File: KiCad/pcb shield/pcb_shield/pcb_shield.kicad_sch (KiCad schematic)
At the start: 3 parts, among them J1 Raspberry Pi Zero, U1 BOB-09056

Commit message: add main parts
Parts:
- added A?: Motor Controller Left, Module:Pololu_Breakout-16_15.2x20.3mm, symbol Driver_Motor:Pololu_Breakout_A4988
- added A?: Motor Controller Right, Module:Pololu_Breakout-16_15.2x20.3mm, symbol Driver_Motor:Pololu_Breakout_A4988
- added U? (x3): BOB-09056, BOB-09056:MODULE_BOB-09056, symbol BOB-09056:BOB-09056
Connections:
- net 4 is gone; now on an unnamed net: J1.4 (Pin_4)
- net 14 TXD: now also A1.15 (D0/RX)
- net 18 RXD: now also A1.16 (D1/TX)
- net GND: no longer J1.20 (Pin_20)
- net at U1.JP3-1 (GND): now also J1.20 (Pin_20), U?.JP3-1 (GND), U?.JP3-1 (GND), U?.JP3-1 (GND)
- net at U1.JP3-2 (VCC): now also A1.5 (+5V), U?.JP3-2 (VCC), U?.JP3-2 (VCC), U?.JP3-2 (VCC)
- net at U1.JP3-4 (S0): now also U?.JP3-4 (S0)
- net at U1.JP3-5 (S1): now also U?.JP3-5 (S1)
- net at U1.JP3-6 (S2): now also U?.JP3-6 (S2)
- net at U1.JP3-7 (S3): now also U?.JP3-7 (S3)
- net at U1.JP3-8 (COM): now also U?.JP3-8 (COM)
- net at A1.17 (D2): now also A?.15 (STEP)
- net at A1.23 (D8): now also A?.9 (~{ENABLE}), A?.9 (~{ENABLE})
- net 17: no longer names the net of J1.6 (Pin_6)
- net 17: now also U?.JP3-3 (EN)
- net 22: no longer names the net of J1.8 (Pin_8)
- net 22: now also U?.JP3-3 (EN)
- net 27: no longer names the net of J1.7 (Pin_7)
- net 27: now also U?.JP3-3 (EN)
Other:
- moved on the sheet: A1, J1, U1

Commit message: start with pcb
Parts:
- added C1, C2: C, Capacitor_THT:CP_Radial_D5.0mm_P2.50mm, symbol Device:C
- added J1, J2, J3, J4, J5, J6, J7, J8: (no value), Connector_PinHeader_2.54mm:PinHeader_2x04_P2.54mm_Vertical, symbol Connector_Generic:Conn_02x04_Counter_Clockwise
- added J10, J11: Motor Conn, Connector_PinHeader_2.54mm:PinHeader_1x04_P2.54mm_Vertical, symbol Connector_Generic:Conn_01x04
- added J12: Endstop X, Connector_PinHeader_2.54mm:PinHeader_1x02_P2.54mm_Vertical, symbol Connector_Generic:Conn_01x02
- added J13: Endstop Y, Connector_PinHeader_2.54mm:PinHeader_1x02_P2.54mm_Vertical, symbol Connector_Generic:Conn_01x02
- added J14: Barrel_Jack, symbol Connector:Barrel_Jack
- added J9: E_Magnet, Connector_PinHeader_2.54mm:PinHeader_1x02_P2.54mm_Vertical, symbol Connector_Generic:Conn_01x02
- added Q1: TIP120, Package_TO_SOT_THT:TO-220-3_Vertical, symbol Transistor_BJT:TIP120
- gave numbers to parts that had none: 5
- renumbered J1 to A1, A1 to A2
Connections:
- net 5V: now also U1.JP3-2 (VCC), U2.JP3-2 (VCC), U3.JP3-2 (VCC), U4.JP3-2 (VCC)
- net at U3.JP1-1 (C0): now also J5.1 (Pin_1)
- net at U3.JP1-10 (C9): now also J6.8 (Pin_8)
- net at U3.JP1-11 (C10): now also J6.2 (Pin_2)
- net at U3.JP1-12 (C11): now also J6.7 (Pin_7)
- net at U3.JP1-13 (C12): now also J6.3 (Pin_3)
- net at U3.JP1-14 (C13): now also J6.6 (Pin_6)
- net at U3.JP1-15 (C14): now also J6.4 (Pin_4)
- net at U3.JP1-16 (C15): now also J6.5 (Pin_5)
- net at U3.JP1-2 (C1): now also J5.8 (Pin_8)
- net at U3.JP1-3 (C2): now also J5.2 (Pin_2)
- net at U3.JP1-4 (C3): now also J5.7 (Pin_7)
- net at U3.JP1-5 (C4): now also J5.3 (Pin_3)
- net at U3.JP1-6 (C5): now also J5.6 (Pin_6)
- net at U3.JP1-7 (C6): now also J5.4 (Pin_4)
- net at U3.JP1-8 (C7): now also J5.5 (Pin_5)
- net at U3.JP1-9 (C8): now also J6.1 (Pin_1)
- net at U3.JP3-4 (S0): now also U1.JP3-4 (S0), U2.JP3-4 (S0)
- net at U3.JP3-5 (S1): now also U1.JP3-5 (S1), U2.JP3-5 (S1)
- net at U3.JP3-6 (S2): now also U1.JP3-6 (S2), U2.JP3-6 (S2)
- net at U3.JP3-7 (S3): now also U1.JP3-7 (S3), U2.JP3-7 (S3)
- net at U3.JP3-8 (COM): now also U1.JP3-8 (COM), U2.JP3-8 (COM)
- net at U1.JP1-1 (C0): now also J1.1 (Pin_1)
- net at U1.JP1-10 (C9): now also J2.8 (Pin_8)
- net at U1.JP1-11 (C10): now also J2.2 (Pin_2)
- net at U1.JP1-12 (C11): now also J2.7 (Pin_7)
- net at U1.JP1-13 (C12): now also J2.3 (Pin_3)
- net at U1.JP1-14 (C13): now also J2.6 (Pin_6)
- net at U1.JP1-15 (C14): now also J2.4 (Pin_4)
- net at U1.JP1-16 (C15): now also J2.5 (Pin_5)
- net at U1.JP1-2 (C1): now also J1.8 (Pin_8)
- net at U1.JP1-3 (C2): now also J1.2 (Pin_2)
- net at U1.JP1-4 (C3): now also J1.7 (Pin_7)
- net at U1.JP1-5 (C4): now also J1.3 (Pin_3)
- net at U1.JP1-6 (C5): now also J1.6 (Pin_6)
- net at U1.JP1-7 (C6): now also J1.4 (Pin_4)
- net at U1.JP1-8 (C7): now also J1.5 (Pin_5)
- net at U1.JP1-9 (C8): now also J2.1 (Pin_1)
- net at A3.1 (GND): now also A2.7 (GND), A4.1 (GND), J12.2 (Pin_2), J13.2 (Pin_2)
- net at A3.16 (DIR): now also A2.20 (D5)
- net at A3.2 (VDD): now also A2.5 (+5V), A4.2 (VDD)
- net at A3.3 (1B): now also J10.1 (Pin_1)
- net at A3.4 (1A): now also J10.2 (Pin_2)
- net at A3.5 (2A): now also J10.3 (Pin_3)
- net at A3.6 (2B): now also J10.4 (Pin_4)
- net at A3.7 (GND): now also A4.7 (GND), C1.2, C2.2, J14.1, J9.1 (Pin_1)
- net at A3.8 (VMOT): now also A4.8 (VMOT), C1.1, C2.1, J14.2, Q1.2 (C)
- net at A4.15 (STEP): now also A2.18 (D3)
- net at A4.16 (DIR): now also A2.21 (D6)
- net at A4.3 (1B): now also J11.1 (Pin_1)
- net at A4.4 (1A): now also J11.2 (Pin_2)
- net at A4.5 (2A): now also J11.3 (Pin_3)
- net at A4.6 (2B): now also J11.4 (Pin_4)
- net at U4.JP1-1 (C0): now also J7.1 (Pin_1)
- net at U4.JP1-10 (C9): now also J8.8 (Pin_8)
- net at U4.JP1-11 (C10): now also J8.2 (Pin_2)
- net at U4.JP1-12 (C11): now also J8.7 (Pin_7)
- net at U4.JP1-13 (C12): now also J8.3 (Pin_3)
- net at U4.JP1-14 (C13): now also J8.6 (Pin_6)
- net at U4.JP1-15 (C14): now also J8.4 (Pin_4)
- net at U4.JP1-16 (C15): now also J8.5 (Pin_5)
- net at U4.JP1-2 (C1): now also J7.8 (Pin_8)
- net at U4.JP1-3 (C2): now also J7.2 (Pin_2)
- net at U4.JP1-4 (C3): now also J7.7 (Pin_7)
- net at U4.JP1-5 (C4): now also J7.3 (Pin_3)
- net at U4.JP1-6 (C5): now also J7.6 (Pin_6)
- net at U4.JP1-7 (C6): now also J7.4 (Pin_4)
- net at U4.JP1-8 (C7): now also J7.5 (Pin_5)
- net at U4.JP1-9 (C8): now also J8.1 (Pin_1)
- net at U2.JP1-1 (C0): now also J3.1 (Pin_1)
- net at U2.JP1-10 (C9): now also J4.8 (Pin_8)
- net at U2.JP1-11 (C10): now also J4.2 (Pin_2)
- net at U2.JP1-12 (C11): now also J4.7 (Pin_7)
- net at U2.JP1-13 (C12): now also J4.3 (Pin_3)
- net at U2.JP1-14 (C13): now also J4.6 (Pin_6)
- net at U2.JP1-15 (C14): now also J4.4 (Pin_4)
- net at U2.JP1-16 (C15): now also J4.5 (Pin_5)
- net at U2.JP1-2 (C1): now also J3.8 (Pin_8)
- net at U2.JP1-3 (C2): now also J3.2 (Pin_2)
- net at U2.JP1-4 (C3): now also J3.7 (Pin_7)
- net at U2.JP1-5 (C4): now also J3.3 (Pin_3)
- net at U2.JP1-6 (C5): now also J3.6 (Pin_6)
- net at U2.JP1-7 (C6): now also J3.4 (Pin_4)
- net at U2.JP1-8 (C7): now also J3.5 (Pin_5)
- net at U2.JP1-9 (C8): now also J4.1 (Pin_1)
- net at A2.24 (D9): now also J12.1 (Pin_1)
- net at A2.25 (D10): now also J13.1 (Pin_1)
- net at A2.26 (D11): now also Q1.1 (B)
- new net: J9.2 (Pin_2), Q1.3 (E)
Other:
- moved on the sheet: A1, A2, A3, A4, U1, U2, U3, U4

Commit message: adding multiplexers
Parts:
- removed J1, J2, J3, J4, J5, J6, J7, J8: (no value), Connector_PinHeader_2.54mm:PinHeader_2x04_P2.54mm_Vertical, symbol Connector_Generic:Conn_02x04_Counter_Clockwise
- added J1, J2, J3, J4, J5, J6, J7, J8: (no value), Connector_PinHeader_2.54mm:PinHeader_2x04_P2.54mm_Vertical, symbol Connector_Generic:Conn_02x04_Odd_Even
- J10: value Motor Conn -> Motor Conn L
- J11: value Motor Conn -> Motor Conn R
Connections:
- net at U1.JP1-9 (C8): now also J2.1 (Pin_1)
- net at U1.JP1-11 (C10): now also J2.5 (Pin_5)
- net at U1.JP1-13 (C12): now also J2.8 (Pin_8)
- net at U1.JP1-15 (C14): now also J2.4 (Pin_4)
- net at U1.JP1-16 (C15): now also J2.2 (Pin_2)
- net at U1.JP1-14 (C13): now also J2.6 (Pin_6)
- net at U1.JP1-12 (C11): now also J2.7 (Pin_7)
- net at U1.JP1-10 (C9): now also J2.3 (Pin_3)
- net at U2.JP1-9 (C8): now also J4.1 (Pin_1)
- net at U2.JP1-11 (C10): now also J4.5 (Pin_5)
- net at U2.JP1-13 (C12): now also J4.8 (Pin_8)
- net at U2.JP1-15 (C14): now also J4.4 (Pin_4)
- net at U2.JP1-16 (C15): now also J4.2 (Pin_2)
- net at U2.JP1-14 (C13): now also J4.6 (Pin_6)
- net at U2.JP1-12 (C11): now also J4.7 (Pin_7)
- net at U2.JP1-10 (C9): now also J4.3 (Pin_3)
- net at U3.JP1-1 (C0): now also J5.1 (Pin_1)
- net at U3.JP1-10 (C9): now also J6.3 (Pin_3)
- net at U3.JP1-11 (C10): now also J6.5 (Pin_5)
- net at U3.JP1-12 (C11): now also J6.7 (Pin_7)
- net at U3.JP1-13 (C12): now also J6.8 (Pin_8)
- net at U3.JP1-14 (C13): now also J6.6 (Pin_6)
- net at U3.JP1-15 (C14): now also J6.4 (Pin_4)
- net at U3.JP1-16 (C15): now also J6.2 (Pin_2)
- net at U3.JP1-2 (C1): now also J5.3 (Pin_3)
- net at U3.JP1-3 (C2): now also J5.5 (Pin_5)
- net at U3.JP1-4 (C3): now also J5.7 (Pin_7)
- net at U3.JP1-5 (C4): now also J5.8 (Pin_8)
- net at U3.JP1-6 (C5): now also J5.6 (Pin_6)
- net at U3.JP1-7 (C6): now also J5.4 (Pin_4)
- net at U3.JP1-8 (C7): now also J5.2 (Pin_2)
- net at U3.JP1-9 (C8): now also J6.1 (Pin_1)
- net at U1.JP3-4 (S0), U2.JP3-4 (S0), U3.JP3-4 (S0): now also U4.JP3-4 (S0)
- net at U1.JP3-5 (S1), U2.JP3-5 (S1), U3.JP3-5 (S1): now also U4.JP3-5 (S1)
- net at U1.JP3-6 (S2), U2.JP3-6 (S2), U3.JP3-6 (S2): now also U4.JP3-6 (S2)
- net at U1.JP3-7 (S3), U2.JP3-7 (S3), U3.JP3-7 (S3): now also U4.JP3-7 (S3)
- net at U1.JP3-8 (COM), U2.JP3-8 (COM), U3.JP3-8 (COM): now also U4.JP3-8 (COM)
- net at U1.JP1-1 (C0): now also J1.1 (Pin_1)
- net at U1.JP1-2 (C1): now also J1.3 (Pin_3)
- net at U1.JP1-3 (C2): now also J1.5 (Pin_5)
- net at U1.JP1-4 (C3): now also J1.7 (Pin_7)
- net at U1.JP1-5 (C4): now also J1.8 (Pin_8)
- net at U1.JP1-6 (C5): now also J1.6 (Pin_6)
- net at U1.JP1-7 (C6): now also J1.4 (Pin_4)
- net at U1.JP1-8 (C7): now also J1.2 (Pin_2)
- net at U4.JP1-9 (C8): now also J8.1 (Pin_1)
- net at U4.JP1-11 (C10): now also J8.5 (Pin_5)
- net at U4.JP1-13 (C12): now also J8.8 (Pin_8)
- net at U4.JP1-15 (C14): now also J8.4 (Pin_4)
- net at U4.JP1-16 (C15): now also J8.2 (Pin_2)
- net at U4.JP1-14 (C13): now also J8.6 (Pin_6)
- net at U4.JP1-12 (C11): now also J8.7 (Pin_7)
- net at U4.JP1-10 (C9): now also J8.3 (Pin_3)
- net at U4.JP1-1 (C0): now also J7.1 (Pin_1)
- net at U4.JP1-3 (C2): now also J7.5 (Pin_5)
- net at U4.JP1-5 (C4): now also J7.8 (Pin_8)
- net at U4.JP1-7 (C6): now also J7.4 (Pin_4)
- net at U4.JP1-8 (C7): now also J7.2 (Pin_2)
- net at U4.JP1-6 (C5): now also J7.6 (Pin_6)
- net at U4.JP1-4 (C3): now also J7.7 (Pin_7)
- net at U4.JP1-2 (C1): now also J7.3 (Pin_3)
- net at U2.JP1-1 (C0): now also J3.1 (Pin_1)
- net at U2.JP1-3 (C2): now also J3.5 (Pin_5)
- net at U2.JP1-5 (C4): now also J3.8 (Pin_8)
- net at U2.JP1-7 (C6): now also J3.4 (Pin_4)
- net at U2.JP1-8 (C7): now also J3.2 (Pin_2)
- net at U2.JP1-6 (C5): now also J3.6 (Pin_6)
- net at U2.JP1-4 (C3): now also J3.7 (Pin_7)
- net at U2.JP1-2 (C1): now also J3.3 (Pin_3)

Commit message: almost finished pcb
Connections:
- net 13 is gone; now on an unnamed net: A1.17 (Pin_17)
- net 19 is gone; now on an unnamed net: A1.18 (Pin_18)
- net 26 is gone; now on an unnamed net: A1.19 (Pin_19)
- net 5 is gone; now on an unnamed net: A1.15 (Pin_15)
- net 6 is gone; now on an unnamed net: A1.16 (Pin_16)
- net at U1.JP3-3 (EN): now also A1.8 (Pin_8); no longer A1.4 (Pin_4)
- net at U4.JP3-3 (EN): now also A1.4 (Pin_4); no longer A1.8 (Pin_8)

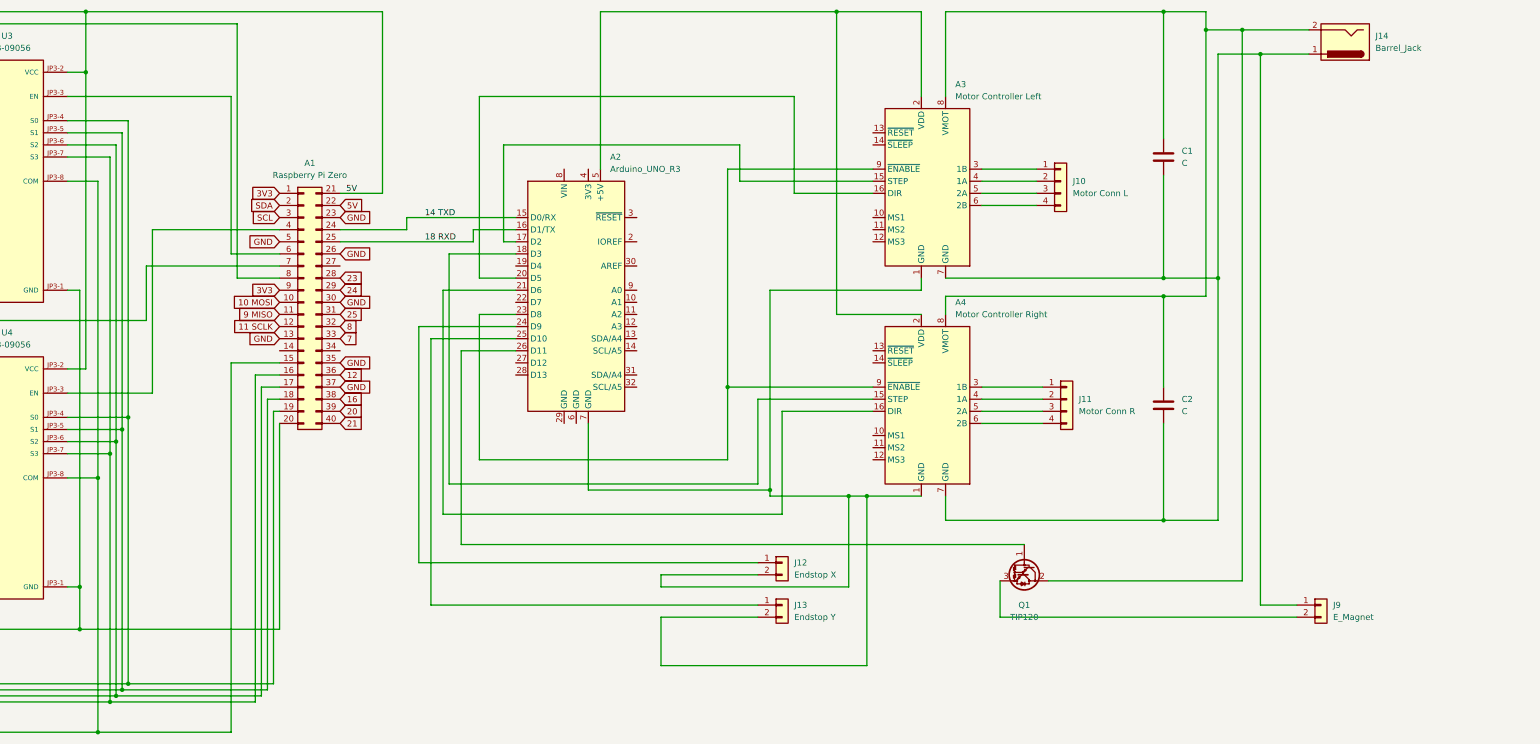
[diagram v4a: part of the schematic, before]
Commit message: add aditional headers
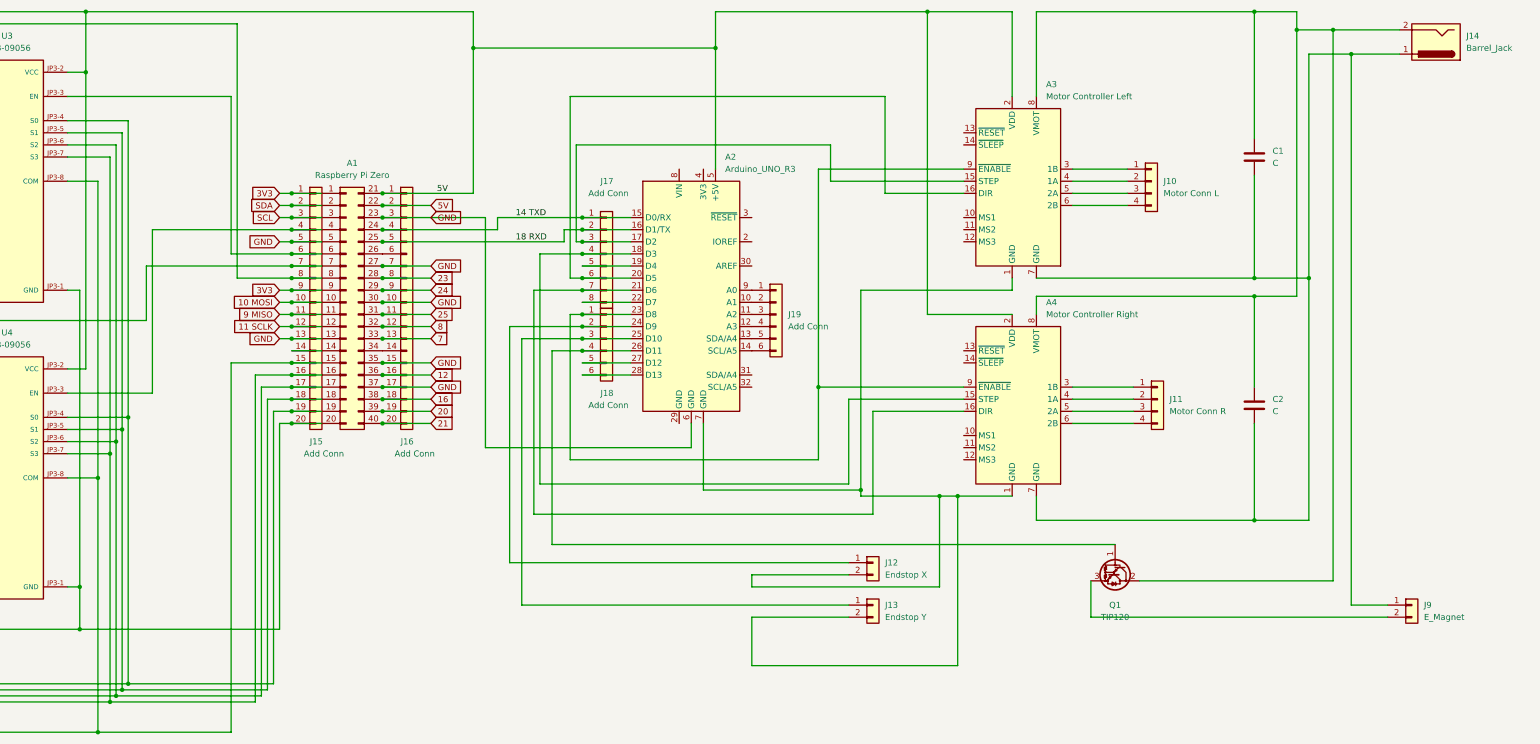
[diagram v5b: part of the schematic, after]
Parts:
- added J15, J16: Add Conn, Connector_PinSocket_2.54mm:PinSocket_1x20_P2.54mm_Vertical, symbol Connector_Generic:Conn_01x20
- added J17: Add Conn, Connector_PinHeader_2.54mm:PinHeader_1x08_P2.54mm_Vertical, symbol Connector_Generic:Conn_01x08
- added J18, J19: Add Conn, Connector_PinHeader_2.54mm:PinHeader_1x06_P2.54mm_Vertical, symbol Connector_Generic:Conn_01x06
- J14: footprint (none) -> TerminalBlock_Phoenix:TerminalBlock_Phoenix_MKDS-1,5-2_1x02_P5.00mm_Horizontal
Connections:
- net 10 MOSI: now also J15.10 (Pin_10)
- net 11 SCLK: now also J15.12 (Pin_12)
- net 12: now also J16.16 (Pin_16)
- net 14 TXD: now also J16.4 (Pin_4), J17.1 (Pin_1)
- net 16: now also J16.18 (Pin_18)
- net 18 RXD: now also J16.5 (Pin_5), J17.2 (Pin_2)
- net 20: now also J16.19 (Pin_19)
- net 21: now also J16.20 (Pin_20)
- net 23: now also J16.8 (Pin_8)
- net 24: now also J16.9 (Pin_9)
- net 25: now also J16.11 (Pin_11)
- net 3V3: now also J15.1 (Pin_1), J15.9 (Pin_9)
- net 5V: now also A2.5 (+5V), A3.2 (VDD), A4.2 (VDD), J16.1 (Pin_1), J16.2 (Pin_2)
- net 7: now also J16.13 (Pin_13)
- net 8: now also J16.12 (Pin_12)
- net 9 MISO: now also J15.11 (Pin_11)
- net GND: now also A1.27 (Pin_27), A2.6 (GND), J15.13 (Pin_13), J15.5 (Pin_5), J16.10 (Pin_10), J16.15 (Pin_15), J16.17 (Pin_17), J16.3 (Pin_3), J16.7 (Pin_7); no longer A1.26 (Pin_26)
- net SCL: now also J15.3 (Pin_3)
- net SDA: now also J15.2 (Pin_2)
- net at A2.25 (D10), J13.1 (Pin_1): now also J18.3 (Pin_3)
- net at A1.20 (Pin_20), U1.JP3-1 (GND), U2.JP3-1 (GND)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: now also J15.20 (Pin_20)
- net at A1.6 (Pin_6), U3.JP3-3 (EN): now also J15.6 (Pin_6)
- net at A1.19 (Pin_19), U1.JP3-4 (S0), U2.JP3-4 (S0)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: now also J15.19 (Pin_19)
- net at A1.18 (Pin_18), U1.JP3-5 (S1), U2.JP3-5 (S1)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: now also J15.18 (Pin_18)
- net at A1.17 (Pin_17), U1.JP3-6 (S2), U2.JP3-6 (S2)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: now also J15.17 (Pin_17)
- net at A1.16 (Pin_16), U1.JP3-7 (S3), U2.JP3-7 (S3)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: now also J15.16 (Pin_16)
- net at A1.15 (Pin_15), U1.JP3-8 (COM), U2.JP3-8 (COM)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: now also J15.15 (Pin_15)
- net at A1.8 (Pin_8), U1.JP3-3 (EN): now also J15.8 (Pin_8)
- net at A2.17 (D2), A3.15 (STEP): now also J17.3 (Pin_3)
- net at A2.20 (D5), A3.16 (DIR): now also J17.6 (Pin_6)
- net at A2.23 (D8), A3.9 (~{ENABLE}), A4.9 (~{ENABLE}): now also J18.1 (Pin_1)
- net at A2.24 (D9), J12.1 (Pin_1): now also J18.2 (Pin_2)
- net at A2.18 (D3), A4.15 (STEP): now also J17.4 (Pin_4)
- net at A2.21 (D6), A4.16 (DIR): now also J17.7 (Pin_7)
- net at A1.4 (Pin_4), U4.JP3-3 (EN): now also J15.4 (Pin_4)
- net at A1.7 (Pin_7), U2.JP3-3 (EN): now also J15.7 (Pin_7)
- net at A2.26 (D11), Q1.1 (B): now also J18.4 (Pin_4)
- net at A1.14 (Pin_14): now also J15.14 (Pin_14)
- net at A1.34 (Pin_34): now also J16.14 (Pin_14)
- net at A2.10 (A1): now also J19.2 (Pin_2)
- net at A2.11 (A2): now also J19.3 (Pin_3)
- net at A2.12 (A3): now also J19.4 (Pin_4)
- net at A2.13 (SDA/A4): now also J19.5 (Pin_5)
- net at A2.14 (SCL/A5): now also J19.6 (Pin_6)
- net at A2.19 (D4): now also J17.5 (Pin_5)
- net at A2.22 (D7): now also J17.8 (Pin_8)
- net at A2.27 (D12): now also J18.5 (Pin_5)
- net at A2.28 (D13): now also J18.6 (Pin_6)
- net at A2.9 (A0): now also J19.1 (Pin_1)
- new net: A1.26 (Pin_26), J16.6 (Pin_6)
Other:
- moved on the sheet: A1, A2, A3, A4, C1, C2, J10, J11, J12, J13, J14, J9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
